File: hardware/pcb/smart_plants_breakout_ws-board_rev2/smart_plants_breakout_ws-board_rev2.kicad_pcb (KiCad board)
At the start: 2 copper layers, 48 x 70 mm, 27 parts, among them J1 Conn_01x09_Pin, J2 Conn_01x09_Pin, Q1 IRLZ14, U1 Waveshare ESP32-C6-Nano

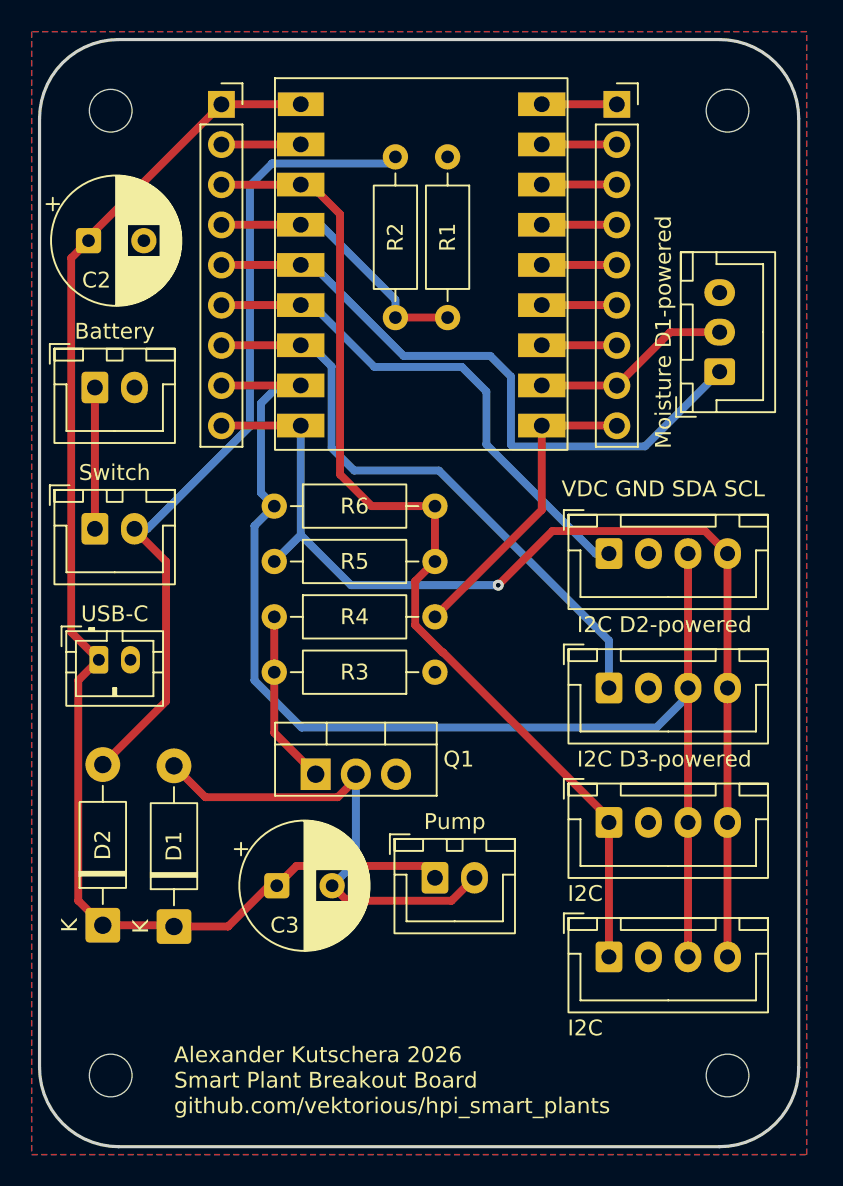
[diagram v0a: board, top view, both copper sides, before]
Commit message: changed pins
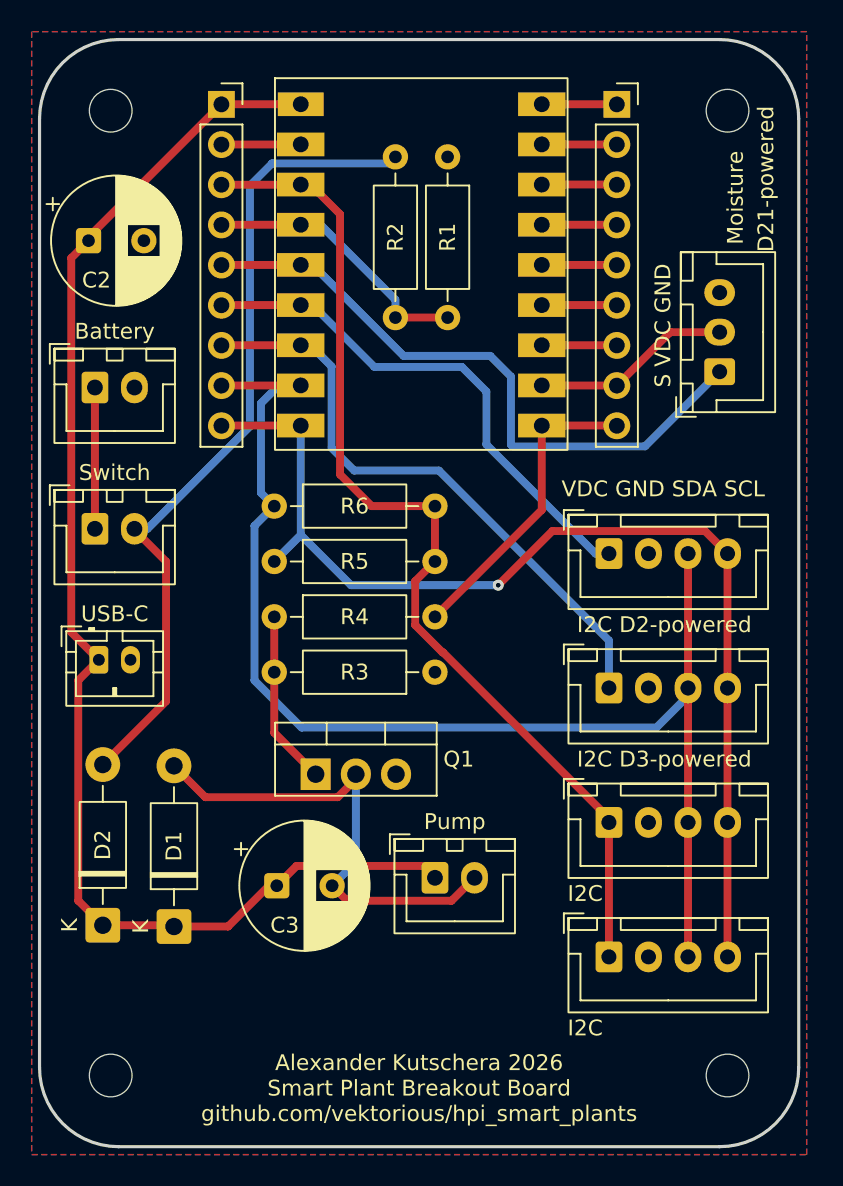
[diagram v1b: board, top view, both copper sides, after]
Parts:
- Moisture: renamed from Moisture D1-powered
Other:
- board text added: "D21-powered"
- board text added: "S VDC GND"
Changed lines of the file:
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@@
 		(descr "JST XH series connector, B3B-XH-A (http://www.jst-mfg.com/product/pdf/eng/eXH.pdf), generated with kicad-footprint-generator")
 		(tags "connector JST XH vertical")
-		(property "Reference" "Moisture D1-powered"
-			(at 2.5 -3.55 90)
+		(property "Reference" "Moisture"
+			(at 11 1 90)
 			(layer "F.SilkS")
 			(effects
@@
 		)
 	)
+	(gr_text "D21-powered"
+		(at 76.51 43.44 90)
+		(layer "F.SilkS")
+		(effects
+			(font
+				(size 1 1)
+				(thickness 0.1)
+			)
+			(justify left bottom)
+		)
+	)
 	(gr_text "Alexander Kutschera 2026\nSmart Plant Breakout Board\ngithub.com/vektorious/hpi_smart_plants"
-		(at 38.5 98 0)
+		(at 54 98.5 0)
 		(layer "F.SilkS")
 		(effects
@@
 				(thickness 0.125)
 			)
+			(justify bottom)
+		)
+	)
+	(gr_text "S VDC GND"
+		(at 70 52 90)
+		(layer "F.SilkS")
+		(effects
+			(font
+				(size 1 1)
+				(thickness 0.1)
+			)
 			(justify left bottom)

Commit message: updated PCB files
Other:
- board text added: "Certified Open Source Hardware OSHWA ID: DE000173"
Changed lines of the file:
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@@
+		)
+	)
+	(gr_text "Certified \nOpen Source Hardware\nOSHWA ID: DE000173"
+		(at 54.102 96.52 0)
+		(layer "B.SilkS")
+		(effects
+			(font
+				(size 2 2)
+				(thickness 0.1)
+			)
+			(justify bottom mirror)
 		)
 	)
